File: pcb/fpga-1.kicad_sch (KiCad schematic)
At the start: 1 part, among them U5 XC7A100T-FGG484

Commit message: power restructuring
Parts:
- U5: symbol FPGA_Xilinx_Artix7:XC7A100T-FGG484 -> library:XC7A100T-FGG484
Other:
- moved on the sheet: U5A, U5B, U5H
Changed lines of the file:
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@@
 	(wire
 		(pts
-			(xy 245.11 30.48) (xy 256.54 30.48)
+			(xy 246.38 30.48) (xy 256.54 30.48)
 		)
 		(stroke
@@
 	(wire
 		(pts
-			(xy 245.11 33.02) (xy 256.54 33.02)
+			(xy 246.38 33.02) (xy 256.54 33.02)
 		)
 		(stroke
@@
 	(bus
 		(pts
-			(xy 259.08 25.4) (xy 267.97 25.4)
+			(xy 259.08 25.4) (xy 266.7 25.4)
 		)
 		(stroke
@@
 	(wire
 		(pts
-			(xy 245.11 35.56) (xy 256.54 35.56)
+			(xy 246.38 35.56) (xy 256.54 35.56)
 		)
 		(stroke
@@
 	(wire
 		(pts
-			(xy 245.11 38.1) (xy 256.54 38.1)
+			(xy 246.38 38.1) (xy 256.54 38.1)
 		)
 		(stroke
@@
 	(hierarchical_label "{JTAG}"
 		(shape bidirectional)
-		(at 267.97 25.4 0)
+		(at 266.7 25.4 0)
 		(effects
 			(font
@@
 	)
 	(symbol
-		(lib_id "FPGA_Xilinx_Artix7:XC7A100T-FGG484")
-		(at 120.65 81.28 0)
+		(lib_id "library:XC7A100T-FGG484")
+		(at 121.92 78.74 0)
 		(unit 2)
 		(exclude_from_sim no)
@@
 		(fields_autoplaced yes)
 		(property "Reference" "U5"
-			(at 120.65 22.86 0)
+			(at 121.92 20.32 0)
 			(effects
 				(font
@@
 		)
 		(property "Value" "XC7A100T-FGG484"
-			(at 120.65 25.4 0)
+			(at 121.92 22.86 0)
 			(effects
 				(font
@@
 		)
 		(property "Footprint" "library:Xilinx_FGG484"
-			(at 120.65 81.28 0)
+			(at 121.92 78.74 0)
 			(effects
 				(font
@@
 		)
 		(property "Datasheet" ""
-			(at 120.65 81.28 0)
+			(at 121.92 78.74 0)
 			(effects
 				(font
@@
 		)
 		(property "Description" "Artix 7 T 100 XC7A100T-FGG484"
-			(at 120.65 193.04 0)
+			(at 121.92 190.5 0)
 			(effects
 				(font
@@
 		)
 		(property "Name" ""
-			(at 120.65 81.28 0)
+			(at 121.92 78.74 0)
 			(effects
 				(font
@@
 	)
 	(symbol
-		(lib_id "FPGA_Xilinx_Artix7:XC7A100T-FGG484")
+		(lib_id "library:XC7A100T-FGG484")
 		(at 228.6 81.28 0)
 		(unit 8)
@@
 	)
 	(symbol
-		(lib_id "FPGA_Xilinx_Artix7:XC7A100T-FGG484")
-		(at 38.1 81.28 0)
+		(lib_id "library:XC7A100T-FGG484")
+		(at 40.64 81.28 0)
 		(unit 1)
 		(exclude_from_sim no)
@@
 		(dnp no)
 		(property "Reference" "U5"
-			(at 38.1 22.86 0)
+			(at 40.64 22.86 0)
 			(effects
 				(font
@@
 		)
 		(property "Value" "XC7A100T-FGG484"
-			(at 38.1 25.4 0)
+			(at 40.64 25.4 0)
 			(effects
 				(font
@@
 		)
 		(property "Footprint" "library:Xilinx_FGG484"
-			(at 38.1 81.28 0)
+			(at 40.64 81.28 0)
 			(effects
 				(font
@@
 		)
 		(property "Datasheet" ""
-			(at 38.1 81.28 0)
+			(at 40.64 81.28 0)
 			(effects
 				(font
@@
 		)
 		(property "Description" "Artix 7 T 100 XC7A100T-FGG484"
-			(at 38.1 193.04 0)
+			(at 40.64 193.04 0)
 			(effects
 				(font
@@
 		)
 		(property "Name" ""
-			(at 38.1 81.28 0)
+			(at 40.64 81.28 0)
 			(effects
 				(font

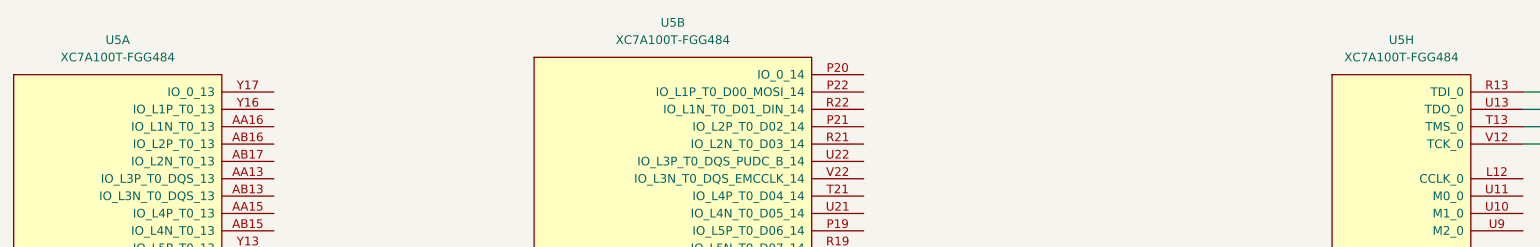
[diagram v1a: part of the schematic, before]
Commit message: moved stuff around, bom
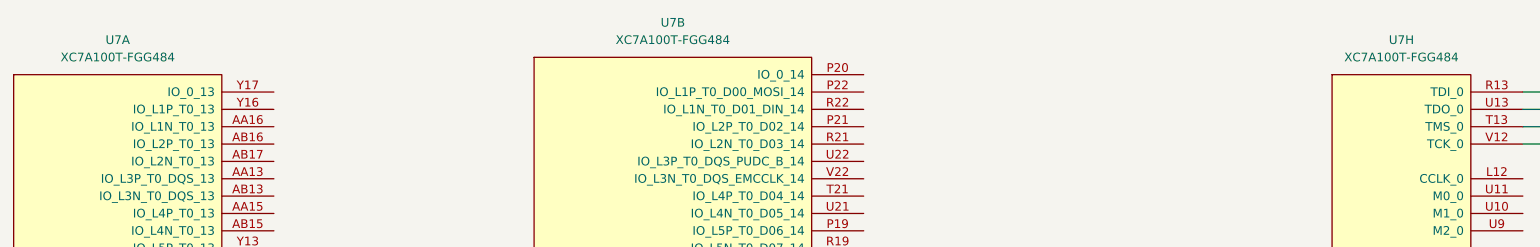
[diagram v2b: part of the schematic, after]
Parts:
- renumbered U5 to U7
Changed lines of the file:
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@@
 		(dnp no)
 		(fields_autoplaced yes)
-		(property "Reference" "U5"
+		(property "Reference" "U7"
 			(at 121.92 20.32 0)
 			(effects
@@
 			(project "RPi-HwAB-1"
 				(path "/e63e39d7-6ac0-4ffd-8aa3-1841a4541b55/59d21473-a004-4514-8090-fd93db818925/350bfe7d-9948-4ca7-a542-a75eb385def4"
-					(reference "U5")
+					(reference "U7")
 					(unit 2)
 				)
@@
 		(dnp no)
 		(fields_autoplaced yes)
-		(property "Reference" "U5"
+		(property "Reference" "U7"
 			(at 228.6 22.86 0)
 			(effects
@@
 			(project "RPi-HwAB-1"
 				(path "/e63e39d7-6ac0-4ffd-8aa3-1841a4541b55/59d21473-a004-4514-8090-fd93db818925/350bfe7d-9948-4ca7-a542-a75eb385def4"
-					(reference "U5")
+					(reference "U7")
 					(unit 8)
 				)
@@
 		(on_board yes)
 		(dnp no)
-		(property "Reference" "U5"
+		(property "Reference" "U7"
 			(at 40.64 22.86 0)
 			(effects
@@
 			(project "RPi-HwAB-1"
 				(path "/e63e39d7-6ac0-4ffd-8aa3-1841a4541b55/59d21473-a004-4514-8090-fd93db818925/350bfe7d-9948-4ca7-a542-a75eb385def4"
-					(reference "U5")
+					(reference "U7")
 					(unit 1)
 				)

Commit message: jtag, dcplng
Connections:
- net DONE: now reaches U7.G11 (DONE_0)
- net PROG_B: now reaches U7.N12 (PROGRAM_B_0)
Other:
- moved on the sheet: U7H
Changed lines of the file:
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@@
 	)
 	(bus_entry
-		(at 256.54 38.1)
+		(at 259.08 53.34)
 		(size 2.54 -2.54)
 		(stroke
@@
 	)
 	(bus_entry
-		(at 256.54 33.02)
+		(at 259.08 35.56)
 		(size 2.54 -2.54)
 		(stroke
@@
 	)
 	(bus_entry
-		(at 256.54 30.48)
+		(at 259.08 30.48)
 		(size 2.54 -2.54)
 		(stroke
@@
 	)
 	(bus_entry
-		(at 256.54 35.56)
+		(at 259.08 58.42)
+		(size 2.54 -2.54)
+		(stroke
+			(width 0)
+			(type default)
+		)
+	)
+	(bus_entry
+		(at 259.08 27.94)
+		(size 2.54 -2.54)
+		(stroke
+			(width 0)
+			(type default)
+		)
+	)
+	(bus_entry
+		(at 259.08 33.02)
 		(size 2.54 -2.54)
 		(stroke
@@
 	(wire
 		(pts
-			(xy 246.38 30.48) (xy 256.54 30.48)
+			(xy 241.3 30.48) (xy 259.08 30.48)
+		)
+		(stroke
+			(width 0)
+			(type default)
+		)
+	)
+	(wire
+		(pts
+			(xy 241.3 27.94) (xy 259.08 27.94)
 		)
 		(stroke
@@
 	(bus
 		(pts
-			(xy 259.08 35.56) (xy 259.08 33.02)
+			(xy 261.62 33.02) (xy 261.62 30.48)
 		)
 		(stroke
@@
 	(wire
 		(pts
-			(xy 246.38 33.02) (xy 256.54 33.02)
+			(xy 241.3 58.42) (xy 259.08 58.42)
+		)
+		(stroke
+			(width 0)
+			(type default)
+		)
+	)
+	(wire
+		(pts
+			(xy 241.3 33.02) (xy 259.08 33.02)
 		)
 		(stroke
@@
 	(bus
 		(pts
-			(xy 259.08 30.48) (xy 259.08 27.94)
+			(xy 261.62 27.94) (xy 261.62 25.4)
 		)
 		(stroke
@@
 	(bus
 		(pts
-			(xy 259.08 25.4) (xy 266.7 25.4)
+			(xy 261.62 22.86) (xy 269.24 22.86)
+		)
+		(stroke
+			(width 0)
+			(type default)
+		)
+	)
+	(bus
+		(pts
+			(xy 261.62 50.8) (xy 261.62 55.88)
 		)
 		(stroke
@@
 	(wire
 		(pts
-			(xy 246.38 35.56) (xy 256.54 35.56)
+			(xy 241.3 53.34) (xy 259.08 53.34)
 		)
 		(stroke
@@
 	(bus
 		(pts
-			(xy 259.08 33.02) (xy 259.08 30.48)
+			(xy 261.62 30.48) (xy 261.62 27.94)
 		)
 		(stroke
@@
 	(wire
 		(pts
-			(xy 246.38 38.1) (xy 256.54 38.1)
+			(xy 241.3 35.56) (xy 259.08 35.56)
 		)
 		(stroke
@@
 	(bus
 		(pts
-			(xy 259.08 27.94) (xy 259.08 25.4)
+			(xy 261.62 25.4) (xy 261.62 22.86)
+		)
+		(stroke
+			(width 0)
+			(type default)
+		)
+	)
+	(bus
+		(pts
+			(xy 261.62 33.02) (xy 261.62 50.8)
 		)
 		(stroke
@@
 	)
 	(label "TDO"
-		(at 254 33.02 180)
+		(at 256.54 30.48 180)
 		(effects
 			(font
@@
 	)
 	(label "TCK"
-		(at 254 38.1 180)
+		(at 256.54 35.56 180)
 		(effects
 			(font
@@
 	)
 	(label "TMS"
-		(at 254 35.56 180)
+		(at 256.54 33.02 180)
 		(effects
 			(font
@@
 		)
 	)
-	(label "TDI"
-		(at 254 30.48 180)
+	(label "DONE"
+		(at 256.54 53.34 180)
 		(effects
 			(font
@@
 		)
 	)
+	(label "TDI"
+		(at 256.54 27.94 180)
+		(effects
+			(font
+				(size 1.27 1.27)
+			)
+			(justify right bottom)
+		)
+	)
+	(label "PROG_B"
+		(at 256.54 58.42 180)
+		(effects
+			(font
+				(size 1.27 1.27)
+			)
+			(justify right bottom)
+		)
+	)
 	(hierarchical_label "{JTAG}"
 		(shape bidirectional)
-		(at 266.7 25.4 0)
+		(at 269.24 22.86 0)
 		(effects
 			(font
@@
 	(symbol
 		(lib_id "library:XC7A100T-FGG484")
-		(at 228.6 81.28 0)
+		(at 223.52 78.74 0)
 		(unit 8)
 		(exclude_from_sim no)
@@
 		(fields_autoplaced yes)
 		(property "Reference" "U7"
-			(at 228.6 22.86 0)
+			(at 223.52 20.32 0)
 			(effects
 				(font
@@
 		)
 		(property "Value" "XC7A100T-FGG484"
-			(at 228.6 25.4 0)
+			(at 223.52 22.86 0)
 			(effects
 				(font
@@
 		)
 		(property "Footprint" "library:Xilinx_FGG484"
-			(at 228.6 81.28 0)
+			(at 223.52 78.74 0)
 			(effects
 				(font
@@
 		)
 		(property "Datasheet" ""
-			(at 228.6 81.28 0)
+			(at 223.52 78.74 0)
 			(effects
 				(font
@@
 		)
 		(property "Description" "Artix 7 T 100 XC7A100T-FGG484"
-			(at 228.6 193.04 0)
+			(at 223.52 190.5 0)
 			(effects
 				(font
@@
 		)
 		(property "Name" ""
-			(at 228.6 81.28 0)
+			(at 223.52 78.74 0)
 			(effects
 				(font

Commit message: qspi
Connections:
- net 3V3_FD: now reaches U7.M14 (VCCO_14)
- net 3V3_FD: now also U7.F12 (VCCO_0), U7.P18 (VCCO_14), U7.R15 (VCCO_14), U7.T12 (VCCO_0), U7.T22 (VCCO_14), U7.U19 (VCCO_14), U7.Y20 (VCCO_14)
- net QSPI0.SIO2: now reaches U7.P21 (IO_L2P_T0_D02_14)
- net QSPI0.SIO0: now reaches U7.P22 (IO_L1P_T0_D00_MOSI_14)
- net QSPI0.SIO3: now reaches U7.R21 (IO_L2N_T0_D03_14)
- net QSPI0.SIO1: now reaches U7.R22 (IO_L1N_T0_D01_DIN_14)
- net QSPI0.CS0n: now reaches U7.T19 (IO_L6P_T0_FCS_B_14)
- net QSPI0.SCLK: now reaches U7.L12 (CCLK_0)

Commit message: decoupling
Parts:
- added C121, C122, C123, C124, C125, C126, C127, C128, C130, C131, C132, C133, C134: 0.1uF, Capacitor_SMD:C_0402_1005Metric, symbol library:C
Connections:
- net 3V3_FD: now also U7.AA17 (VCCO_13), U7.AB14 (VCCO_13), U7.V16 (VCCO_13), U7.W13 (VCCO_13), U7.Y10 (VCCO_13), C121.2, C122.2, C123.2, C124.2, C125.2, C126.2, C127.2, C128.2, C130.2, C131.2, C132.2, C133.2, C134.2
- net PCIE.RST_B: now reaches U7.W21 (IO_L7P_T1_D09_14)
- net GND: now reaches U7.N10 (DXP_0)
- net GND: now also U7.N9 (DXN_0), C121.1, C122.1, C123.1, C124.1, C125.1, C126.1, C127.1, C128.1, C130.1, C131.1, C132.1, C133.1, C134.1

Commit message: bom
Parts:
- C17: renamed from C121; Part Description (none) -> CAP CER 0.1UF 16V X7R 0402
- C18: renamed from C122; Part Description (none) -> CAP CER 0.1UF 16V X7R 0402
- C19: renamed from C123; Part Description (none) -> CAP CER 0.1UF 16V X7R 0402
- C20: renamed from C124; Part Description (none) -> CAP CER 0.1UF 16V X7R 0402
- C21: renamed from C125; Part Description (none) -> CAP CER 0.1UF 16V X7R 0402
- C22: renamed from C126; Part Description (none) -> CAP CER 0.1UF 16V X7R 0402
- C23: renamed from C130; Part Description (none) -> CAP CER 0.1UF 16V X7R 0402
- C24: renamed from C131; Part Description (none) -> CAP CER 0.1UF 16V X7R 0402
- C25: renamed from C132; Part Description (none) -> CAP CER 0.1UF 16V X7R 0402
- C26: renamed from C133; Part Description (none) -> CAP CER 0.1UF 16V X7R 0402
- C27: renamed from C127; Part Description (none) -> CAP CER 0.1UF 16V X7R 0402
- C28: renamed from C134; Part Description (none) -> CAP CER 0.1UF 16V X7R 0402
- C29: renamed from C128; Part Description (none) -> CAP CER 0.1UF 16V X7R 0402
- U7: Manufacturer (none) -> AMD; Manufacturer Product Number (none) -> XC7A100T-1FGG484C; Part Description (none) -> IC FPGA 285 I/O 484FBGA

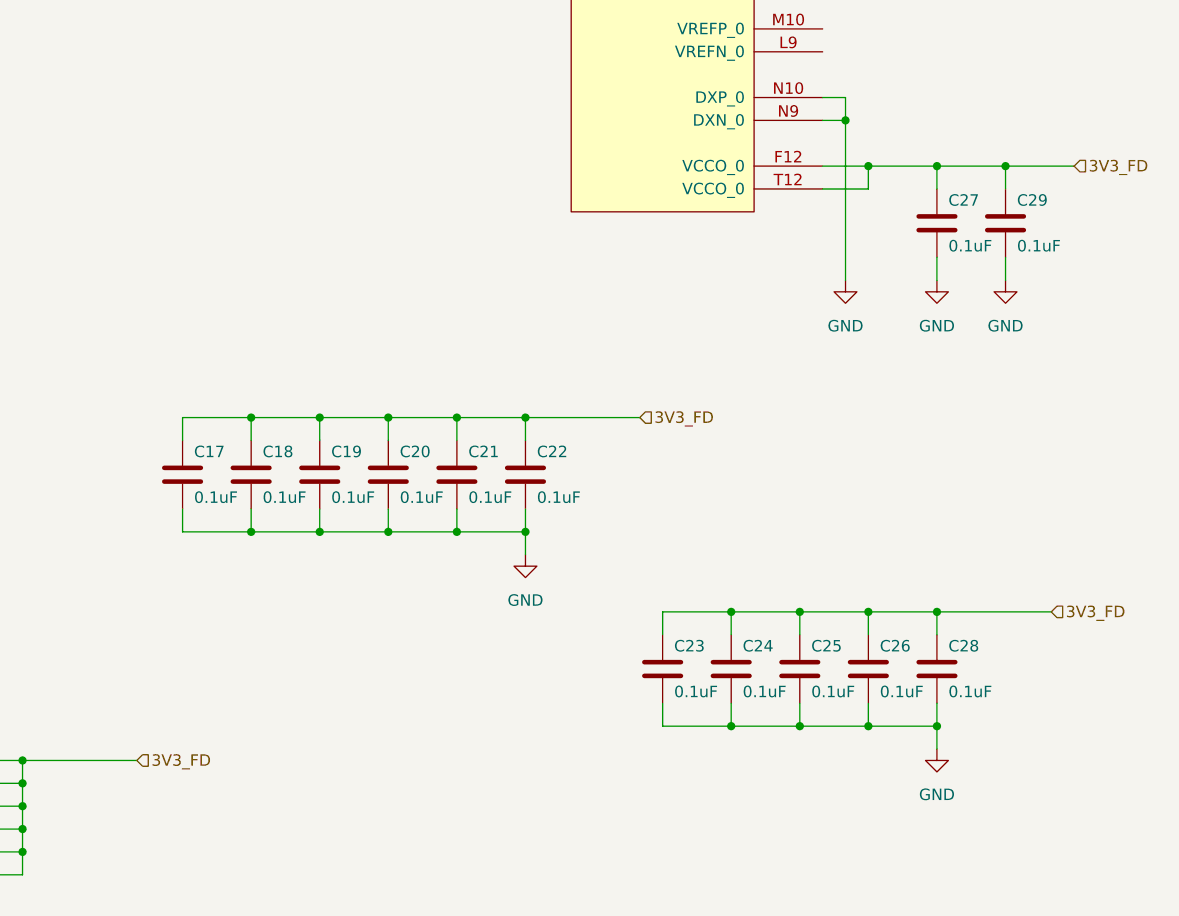
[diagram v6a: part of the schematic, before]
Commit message: added mig ddr pinout constraints
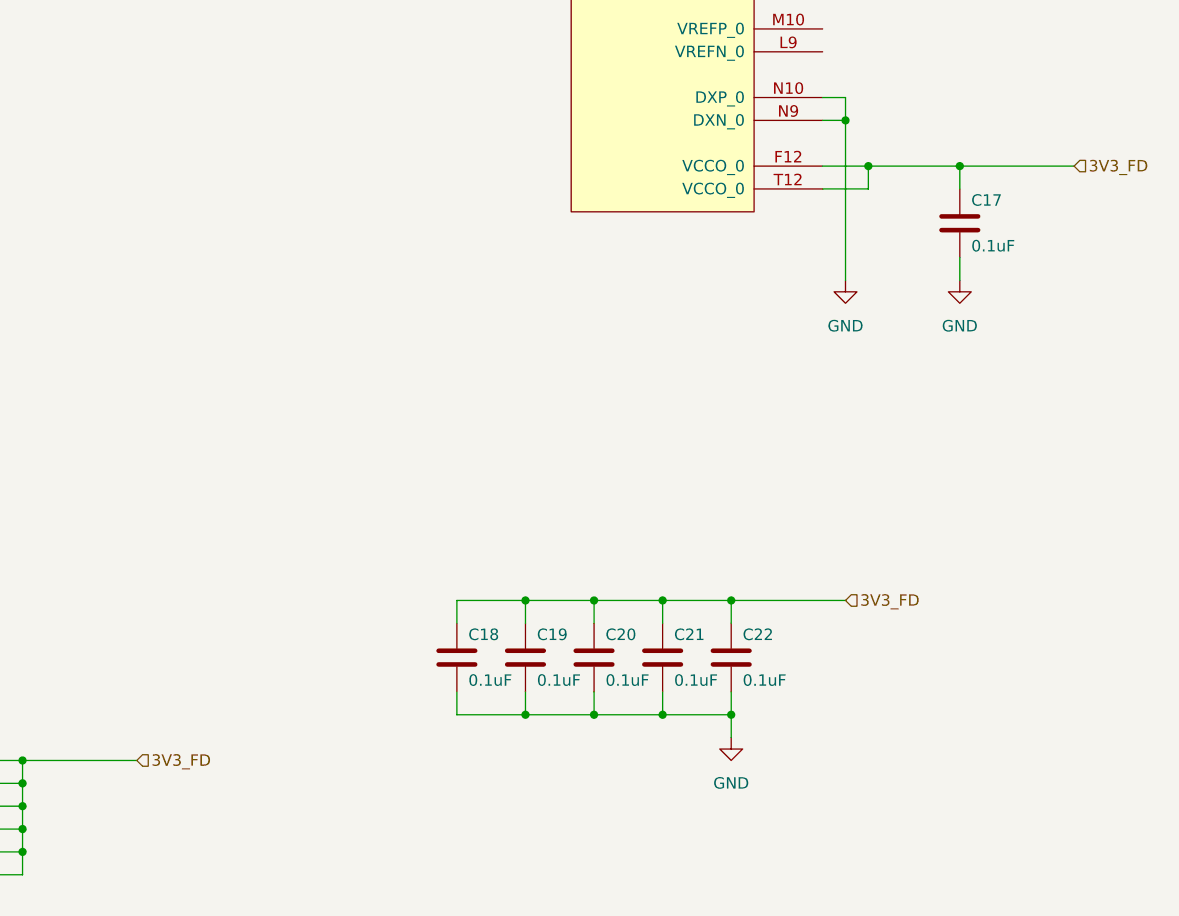
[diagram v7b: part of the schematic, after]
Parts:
- removed C17, C21, C22, C25, C26, C28, C29: 0.1uF, Capacitor_SMD:C_0402_1005Metric, symbol library:C
- renumbered C27 to C17, C23 to C21, C24 to C22
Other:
- moved on the sheet: C17, C21, C22

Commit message: real ddr pinout done
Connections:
- net DDR_SYS_RESET: now reaches U7.AA18 (IO_L17P_T2_A14_D30_14)
- net DDR_INIT_CALIB_COMPLETE: now reaches U7.AA19 (IO_L15P_T2_DQS_RDWR_B_14)
- net DDR_TG_COMPARE_ERROR: now reaches U7.AA20 (IO_L8P_T1_D11_14)
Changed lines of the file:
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@@
+	(wire
+		(pts
+			(xy 149.86 101.6) (xy 180.34 101.6)
+		)
+		(stroke
+			(width 0)
+			(type default)
+		)
+	)
 	(wire
 		(pts
@@
 	(bus
 		(pts
-			(xy 180.34 22.86) (xy 172.72 22.86)
+			(xy 175.26 25.4) (xy 172.72 25.4)
+		)
+		(stroke
+			(width 0)
+			(type default)
+		)
+	)
+	(wire
+		(pts
+			(xy 149.86 66.04) (xy 180.34 66.04)
 		)
 		(stroke
@@
 	(wire
 		(pts
-			(xy 180.34 60.96) (xy 149.86 60.96)
+			(xy 167.64 60.96) (xy 149.86 60.96)
 		)
 		(stroke
@@
 	(bus
 		(pts
-			(xy 261.62 22.86) (xy 269.24 22.86)
+			(xy 261.62 22.86) (xy 264.16 22.86)
 		)
 		(stroke
@@
 	(wire
 		(pts
+			(xy 149.86 111.76) (xy 180.34 111.76)
+		)
+		(stroke
+			(width 0)
+			(type default)
+		)
+	)
+	(wire
+		(pts
 			(xy 223.52 139.7) (xy 223.52 142.24)
 		)
@@
 	(bus
 		(pts
-			(xy 172.72 22.86) (xy 172.72 27.94)
+			(xy 172.72 25.4) (xy 172.72 27.94)
 		)
 		(stroke
@@
 			(width 0)
 			(type default)
+		)
+	)
+	(label "DDR_INIT_CALIB_COMPLETE"
+		(at 180.34 101.6 180)
+		(effects
+			(font
+				(size 1.27 1.27)
+			)
+			(justify right bottom)
 		)
 	)
@@
 		)
 	)
+	(label "DDR_TG_COMPARE_ERROR"
+		(at 180.34 66.04 180)
+		(effects
+			(font
+				(size 1.27 1.27)
+			)
+			(justify right bottom)
+		)
+	)
 	(label "TCK"
 		(at 256.54 35.56 180)
@@
 	(label "TMS"
 		(at 256.54 33.02 180)
+		(effects
+			(font
+				(size 1.27 1.27)
+			)
+			(justify right bottom)
+		)
+	)
+	(label "DDR_SYS_RESET"
+		(at 180.34 111.76 180)
 		(effects
 			(font
@@
 	(hierarchical_label "QSPI0{QSPI}"
 		(shape bidirectional)
-		(at 180.34 22.86 0)
+		(at 175.26 25.4 0)
 		(effects
 			(font
@@
 	(hierarchical_label "PCIE.RST_B"
 		(shape input)
-		(at 180.34 60.96 0)
+		(at 167.64 60.96 0)
 		(effects
 			(font
@@
 	(hierarchical_label "{JTAG}"
 		(shape bidirectional)
-		(at 269.24 22.86 0)
-		(effects
-			(font
+		(at 264.16 22.86 0)
+		(effects
+			(font
